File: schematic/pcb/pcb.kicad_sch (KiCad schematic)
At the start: 1 part, among them U1 ESP32-WROOM-32

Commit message: pcb #2
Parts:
- added U2: NEO-M9N, RF_GPS:ublox_NEO, symbol RF_GPS:NEO-M9N
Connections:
- new net: U2.10 (GND), U2.12 (GND), U2.13 (GND), U2.24 (GND)
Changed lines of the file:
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@@
 (kicad_sch (version 20230121) (generator eeschema)
   (paper "A4")
+  (symbol (lib_id "RF_GPS:NEO-M9N") (at 79.375 61.595 0) (unit 1)
+    (in_bom yes) (on_board yes) (dnp no) (fields_autoplaced)
+    (property "Reference" "U2" (at 81.5691 83.82 0)
+      (effects (font (size 1.27 1.27)) (justify left))
+    )
+    (property "Value" "NEO-M9N" (at 81.5691 86.36 0)
+      (effects (font (size 1.27 1.27)) (justify left))
+    )
+    (property "Footprint" "RF_GPS:ublox_NEO" (at 89.535 83.185 0)
+      (effects (font (size 1.27 1.27)) hide)
+    )
+    (property "Datasheet" "https://www.u-blox.com/sites/default/files/NEO-M9N-00B_DataSheet_UBX-19014285.pdf" (at 79.375 61.595 0)
+      (effects (font (size 1.27 1.27)) hide)
+    )
+    (pin "1")
+    (pin "10")
+    (pin "11")
+    (pin "12")
+    (pin "13")
+    (pin "14")
+    (pin "15")
+    (pin "16")
+    (pin "17")
+    (pin "18")
+    (pin "19")
+    (pin "2")
+    (pin "20")
+    (pin "21")
+    (pin "22")
+    (pin "23")
+    (pin "24")
+    (pin "3")
+    (pin "4")
+    (pin "5")
+    (pin "6")
+    (pin "7")
+    (pin "8")
+    (pin "9")
+    (instances
+      (project "pcb"
+        (path "/bb09d15e-8949-465f-96ce-de682ac5520f"
+          (reference "U2") (unit 1)
+        )
+      )
+    )
+  )
   (symbol (lib_id "RF_Module:ESP32-WROOM-32") (at 140.589 62.357 0) (unit 1)
     (in_bom yes) (on_board yes) (dnp no) (fields_autoplaced)

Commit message: schematic update
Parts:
- added C1: 1004322, RF_GPS:GPS_ANTENNA, symbol GPS_ANTENNA:1004322
- added C2: 0.1uH, symbol Device:C_Small
- added C3: 1uH, symbol Device:C_Small
- added P1: USB_C_Plug_USB2.0, Connector_USB:USB_C_Receptacle_GCT_USB4135-GF-A_6P_TopMnt_Horizontal, symbol Connector:USB_C_Plug_USB2.0
- added R1, R10, R11, R12, R13, R14, R15, R16, R17, R18, R2, R3, R4, R5, R6, R7, R8, R9: R_Small, Resistor_SMD:R_0402_1005Metric_Pad0.72x0.64mm_HandSolder, symbol Device:R_Small
- added U3: CP2102N-Axx-xQFN28, Package_DFN_QFN:QFN-28-1EP_5x5mm_P0.5mm_EP3.35x3.35mm, symbol Interface_USB:CP2102N-Axx-xQFN28
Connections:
- net at U2.1 (~{SAFEBOOT}): now also R8.2
- net at U2.10 (GND), U2.12 (GND), U2.13 (GND)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: now also R18.2
- net at U2.11 (RF_IN): now also R16.1
- net at U2.14 (LNA_EN): now also R15.1
- net at U2.18 (SDA/~{SPI_CS}): now also R5.2
- net at U2.19 (SCL/SPI_CLK): now also R6.2
- net at U2.2 (D_SEL): now also R10.2
- net at U2.20 (TXD/SPI_MISO): now also R3.2
- net at U2.21 (RXD/SPI_MOSI): now also R4.2
- net at U2.22 (V_BCKP): now also R12.1
- net at U2.23 (VCC): now also R11.1
- net at U2.3 (TIMEPULSE): now also R17.1
- net at U2.4 (EXTINT): now also R7.2
- net at U2.5 (USB_DM): now also R1.1
- net at U2.6 (USB_DP): now also R2.2
- net at U2.7 (VDD_USB): now also R13.1
- net at U2.8 (~{RESET}): now also R9.2
- net at U2.9 (VCC_RF): now also R14.1
- net GND: now reaches U1.1 (GND), U1.15 (GND), U1.38 (GND), U1.39 (GND)
- net GND: now also C2.1, C3.2, P1.A1 (GND), P1.A12 (GND), P1.B1 (GND), P1.B12 (GND), P1.S1 (SHIELD), R13.2, R18.1, U3.29 (GND), U3.3 (GND)
- net GPS_MISO: now reaches U1.13 (IO14)
- net GPS_MISO: now also R3.1
- net GPS_SCK: now reaches U1.16 (IO13)
- net GPS_SCK: now also R6.1
- net GPS_MOSI: now reaches U1.27 (IO16)
- net GPS_MOSI: now also R4.1
- net ESP32_RX0: now reaches U1.34 (RXD0/IO3)
- net ESP32_RX0: now also U3.26 (TXD)
- net ESP32_TX0: now reaches U1.35 (TXD0/IO1)
- net ESP32_TX0: now also U3.25 (RXD)
- new net: C1.1, R16.2
- new net: C3.1, P1.A4 (VBUS), P1.A9 (VBUS), P1.B4 (VBUS), P1.B9 (VBUS), U3.7 (VREGIN), U3.8 (VBUS)
- new net: P1.A6 (D+), U3.4 (D+)
- new net: P1.A7 (D-), U3.5 (D-)
- new net +3V3: C2.2, R11.2, R12.2, U3.6 (VDD)
- new net GPS_CS: R5.1
- no-connect marks 0 -> 11
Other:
- note added: "ESP32 WROOM 32"
- note added: "UBLOX M9N"
- note added: "USB <-> UART"
- moved on the sheet: U1, U2

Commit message: schematic udpt
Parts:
- added C4: 10uF, symbol Device:C_Small
- added C5, C6: 0.1uF, symbol Device:C_Small
- added J1: MAV_Serial, Connector_JST:JST_GH_BM04B-GHS-TBT_1x04-1MP_P1.25mm_Vertical, symbol Connector:Conn_01x04_Pin
- added J2: Screen, symbol Connector:Conn_01x06_Pin
- added J3: SERVO_Serial, Connector_JST:JST_GH_BM04B-GHS-TBT_1x04-1MP_P1.25mm_Vertical, symbol Connector:Conn_01x04_Pin
- added J4: MAG_Serial, Connector_JST:JST_GH_BM04B-GHS-TBT_1x04-1MP_P1.25mm_Vertical, symbol Connector:Conn_01x04_Pin
- added R19: 10k, symbol Device:R_Small
- added SW1: BOOT, symbol Switch:SW_Push
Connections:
- net +3V3: now also U1.2 (VDD), C4.1, C5.1, R19.1
- net GND: now also C4.2, C5.2, C6.2, SW1.2
- net GPS_CS: now also U1.23 (IO15)
- net GPS_MISO: now also U1.14 (IO12); no longer U1.13 (IO14)
- net GPS_MOSI: now also U1.16 (IO13); no longer U1.27 (IO16)
- net GPS_SCK: now also U1.13 (IO14); no longer U1.16 (IO13)
- net at U1.25 (IO0): now also SW1.1
- net SCREEN_CS: now reaches U1.29 (IO5)
- net at U1.3 (EN): now also C6.1, R19.2
- net SCREEN_SCK: now reaches U1.30 (IO18)
- net SCREEN_MISO: now reaches U1.31 (IO19)
- net SCREEN_MOSI: now reaches U1.37 (IO23)
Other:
- moved on the sheet: C3, U1

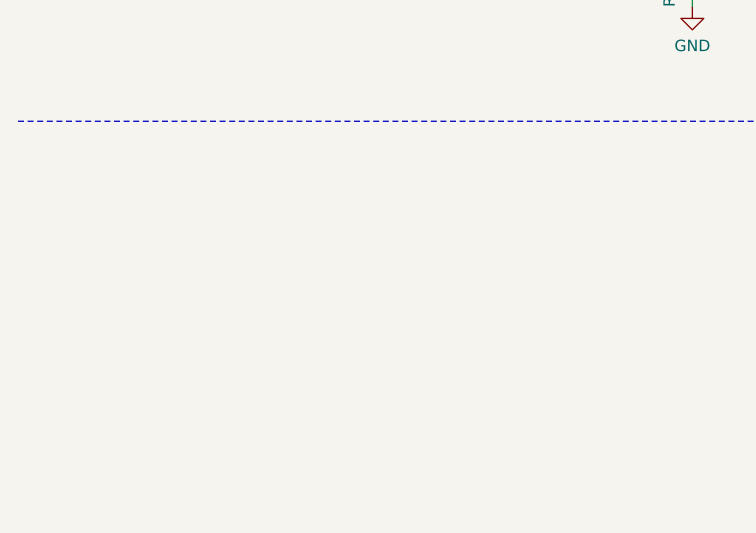
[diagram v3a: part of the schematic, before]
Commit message: ldo added
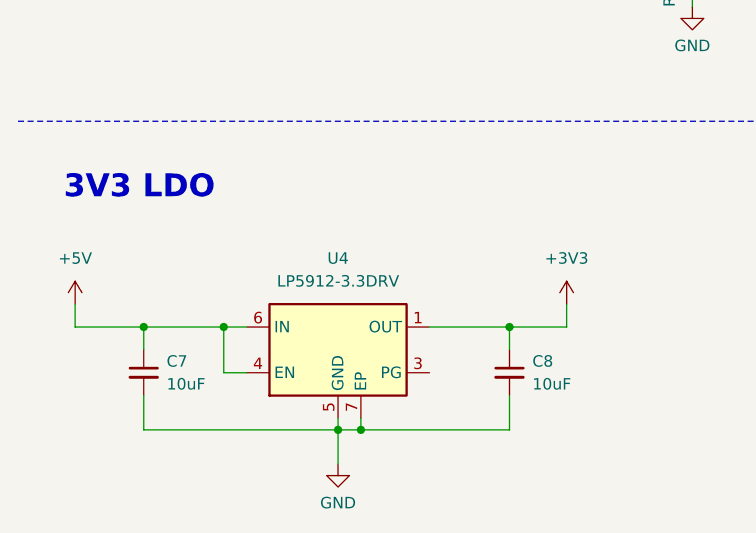
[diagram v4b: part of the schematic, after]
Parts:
- added C7, C8: 10uF, symbol Device:C_Small
- added U4: LP5912-3.3DRV, Package_SON:WSON-6-1EP_2x2mm_P0.65mm_EP1x1.6mm_ThermalVias, symbol Regulator_Linear:LP5912-3.3DRV
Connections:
- net +3V3: now also C8.1, U4.1 (OUT)
- net GND: now also C7.2, C8.2, U4.5 (GND), U4.7 (EP)
- new net +5V: C7.1, U4.4 (EN), U4.6 (IN)
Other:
- note added: "3V3 LDO"
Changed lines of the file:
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@@
   (junction (at 82.55 30.48) (diameter 0) (color 0 0 0 0)
   )
+  (junction (at 67.31 135.89) (diameter 0) (color 0 0 0 0)
+  )
+  (junction (at 48.26 147.32) (diameter 0) (color 0 0 0 0)
+  )
+  (junction (at 50.8 147.32) (diameter 0) (color 0 0 0 0)
+  )
   (junction (at 317.5 83.82) (diameter 0) (color 0 0 0 0)
   )
@@
   )
   (junction (at 204.47 44.45) (diameter 0) (color 0 0 0 0)
+  )
+  (junction (at 26.67 135.89) (diameter 0) (color 0 0 0 0)
+  )
+  (junction (at 35.56 135.89) (diameter 0) (color 0 0 0 0)
   )
   (no_connect (at 332.74 52.07))
@@
     (stroke (width 0) (type default))
   )
+  (wire (pts (xy 67.31 135.89) (xy 67.31 138.43))
+    (stroke (width 0) (type default))
+  )
   (wire (pts (xy 87.63 31.75) (xy 87.63 36.83))
     (stroke (width 0) (type default))
@@
     (stroke (width 0) (type default))
   )
+  (wire (pts (xy 38.1 140.97) (xy 35.56 140.97))
+    (stroke (width 0) (type default))
+  )
   (wire (pts (xy 350.52 34.29) (xy 370.84 34.29))
     (stroke (width 0) (type default))
   )
   (wire (pts (xy 66.04 80.01) (xy 69.85 80.01))
+    (stroke (width 0) (type default))
+  )
+  (wire (pts (xy 67.31 143.51) (xy 67.31 147.32))
     (stroke (width 0) (type default))
   )
@@
     (stroke (width 0) (type dash))
   )
+  (wire (pts (xy 48.26 147.32) (xy 48.26 151.13))
+    (stroke (width 0) (type default))
+  )
+  (wire (pts (xy 58.42 135.89) (xy 67.31 135.89))
+    (stroke (width 0) (type default))
+  )
+  (wire (pts (xy 26.67 143.51) (xy 26.67 147.32))
+    (stroke (width 0) (type default))
+  )
   (wire (pts (xy 172.72 46.99) (xy 185.42 46.99))
     (stroke (width 0) (type default))
@@
     (stroke (width 0) (type default))
   )
+  (wire (pts (xy 50.8 146.05) (xy 50.8 147.32))
+    (stroke (width 0) (type default))
+  )
   (wire (pts (xy 373.38 24.13) (xy 373.38 27.94))
     (stroke (width 0) (type default))
   )
+  (wire (pts (xy 67.31 147.32) (xy 50.8 147.32))
+    (stroke (width 0) (type default))
+  )
+  (wire (pts (xy 48.26 146.05) (xy 48.26 147.32))
+    (stroke (width 0) (type default))
+  )
   (wire (pts (xy 87.63 90.17) (xy 87.63 92.71))
     (stroke (width 0) (type default))
   )
+  (wire (pts (xy 73.66 135.89) (xy 67.31 135.89))
+    (stroke (width 0) (type default))
+  )
   (wire (pts (xy 386.08 41.91) (xy 391.16 41.91))
     (stroke (width 0) (type default))
@@
   )
   (wire (pts (xy 172.72 39.37) (xy 172.72 40.64))
+    (stroke (width 0) (type default))
+  )
+  (wire (pts (xy 26.67 135.89) (xy 26.67 138.43))
     (stroke (width 0) (type default))
   )
@@
     (stroke (width 0) (type default))
   )
+  (wire (pts (xy 35.56 135.89) (xy 26.67 135.89))
+    (stroke (width 0) (type default))
+  )
+  (wire (pts (xy 50.8 147.32) (xy 48.26 147.32))
+    (stroke (width 0) (type default))
+  )
   (polyline (pts (xy 297.18 12.7) (xy 297.18 113.03))
     (stroke (width 0) (type dash))
@@
     (stroke (width 0) (type default))
   )
+  (wire (pts (xy 48.26 147.32) (xy 26.67 147.32))
+    (stroke (width 0) (type default))
+  )
+  (wire (pts (xy 35.56 140.97) (xy 35.56 135.89))
+    (stroke (width 0) (type default))
+  )
   (wire (pts (xy 204.47 50.8) (xy 204.47 53.34))
     (stroke (width 0) (type default))
@@
   )
   (wire (pts (xy 337.82 44.45) (xy 337.82 54.61))
+    (stroke (width 0) (type default))
+  )
+  (wire (pts (xy 73.66 133.35) (xy 73.66 135.89))
     (stroke (width 0) (type default))
   )
@@
     (stroke (width 0) (type default))
   )
+  (wire (pts (xy 19.05 133.35) (xy 19.05 135.89))
+    (stroke (width 0) (type default))
+  )
   (wire (pts (xy 49.53 62.23) (xy 60.96 62.23))
     (stroke (width 0) (type default))
@@
     (stroke (width 0) (type default))
   )
+  (wire (pts (xy 38.1 135.89) (xy 35.56 135.89))
+    (stroke (width 0) (type default))
+  )
   (wire (pts (xy 87.63 41.91) (xy 87.63 44.45))
     (stroke (width 0) (type default))
@@
   )
   (wire (pts (xy 332.74 57.15) (xy 360.68 57.15))
+    (stroke (width 0) (type default))
+  )
+  (wire (pts (xy 19.05 135.89) (xy 26.67 135.89))
     (stroke (width 0) (type default))
   )
@@
   )
   (text "ESP32 WROOM 32" (at 165.1 19.05 0)
+    (effects (font (size 2.54 2.54) (thickness 0.508) bold) (justify left bottom))
+  )
+  (text "3V3 LDO" (at 17.78 121.92 0)
     (effects (font (size 2.54 2.54) (thickness 0.508) bold) (justify left bottom))
   )
@@
     )
   )
+  (symbol (lib_id "Device:C_Small") (at 67.31 140.97 0) (unit 1)
+    (in_bom yes) (on_board yes) (dnp no) (fields_autoplaced)
+    (property "Reference" "C8" (at 69.85 139.7063 0)
+      (effects (font (size 1.27 1.27)) (justify left))
+    )
+    (property "Value" "10uF" (at 69.85 142.2463 0)
+      (effects (font (size 1.27 1.27)) (justify left))
+    )
+    (property "Footprint" "" (at 67.31 140.97 0)
+      (effects (font (size 1.27 1.27)) hide)
+    )
+    (property "Datasheet" "~" (at 67.31 140.97 0)
+      (effects (font (size 1.27 1.27)) hide)
+    )
+    (pin "1")
+    (pin "2")
+    (instances
+      (project "pcb"
+        (path "/bb09d15e-8949-465f-96ce-de682ac5520f"
+          (reference "C8") (unit 1)
+        )
+      )
+    )
+  )
   (symbol (lib_id "Device:C_Small") (at 172.72 43.18 0) (unit 1)
     (in_bom yes) (on_board yes) (dnp no) (fields_autoplaced)
@@
     )
   )
+  (symbol (lib_id "Regulator_Linear:LP5912-3.3DRV") (at 48.26 138.43 0) (unit 1)
+    (in_bom yes) (on_board yes) (dnp no) (fields_autoplaced)
+    (property "Reference" "U4" (at 48.26 128.27 0)
+      (effects (font (size 1.27 1.27)))
+    )
+    (property "Value" "LP5912-3.3DRV" (at 48.26 130.81 0)
+      (effects (font (size 1.27 1.27)))
+    )
+    (property "Footprint" "Package_SON:WSON-6-1EP_2x2mm_P0.65mm_EP1x1.6mm_ThermalVias" (at 48.26 129.54 0)
+      (effects (font (size 1.27 1.27)) hide)
+    )
+    (property "Datasheet" "http://www.ti.com/lit/ds/symlink/lp5912.pdf" (at 48.26 125.73 0)
+      (effects (font (size 1.27 1.27)) hide)
+    )
+    (pin "1")
+    (pin "2")
+    (pin "4")
+    (pin "5")
+    (pin "6")
+    (pin "3")
+    (pin "7")
+    (instances
+      (project "pcb"
+        (path "/bb09d15e-8949-465f-96ce-de682ac5520f"
+          (reference "U4") (unit 1)
+        )
+      )
+    )
+  )
   (symbol (lib_id "power:+3V3") (at 82.55 26.67 0) (unit 1)
     (in_bom yes) (on_board yes) (dnp no) (fields_autoplaced)
@@
         (path "/bb09d15e-8949-465f-96ce-de682ac5520f"
           (reference "C5") (unit 1)
+        )
+      )
+    )
+  )
+  (symbol (lib_id "power:GND") (at 48.26 151.13 0) (unit 1)
+    (in_bom yes) (on_board yes) (dnp no) (fields_autoplaced)
+    (property "Reference" "#PWR017" (at 48.26 157.48 0)
+      (effects (font (size 1.27 1.27)) hide)
+    )
+    (property "Value" "GND" (at 48.26 155.448 0)
+      (effects (font (size 1.27 1.27)))
+    )
+    (property "Footprint" "" (at 48.26 151.13 0)
+      (effects (font (size 1.27 1.27)) hide)
+    )
+    (property "Datasheet" "" (at 48.26 151.13 0)
+      (effects (font (size 1.27 1.27)) hide)
+    )
+    (pin "1")
+    (instances
+      (project "pcb"
+        (path "/bb09d15e-8949-465f-96ce-de682ac5520f"
+          (reference "#PWR017") (unit 1)
         )
       )
@@
         (path "/bb09d15e-8949-465f-96ce-de682ac5520f"
           (reference "U2") (unit 1)
+        )
+      )
+    )
+  )
+  (symbol (lib_id "power:+5V") (at 19.05 133.35 0) (unit 1)
+    (in_bom yes) (on_board yes) (dnp no) (fields_autoplaced)
+    (property "Reference" "#PWR016" (at 19.05 137.16 0)
+      (effects (font (size 1.27 1.27)) hide)
+    )
+    (property "Value" "+5V" (at 19.05 128.27 0)
+      (effects (font (size 1.27 1.27)))
+    )
+    (property "Footprint" "" (at 19.05 133.35 0)
+      (effects (font (size 1.27 1.27)) hide)
+    )
+    (property "Datasheet" "" (at 19.05 133.35 0)
+      (effects (font (size 1.27 1.27)) hide)
+    )
+    (pin "1")
+    (instances
+      (project "pcb"
+        (path "/bb09d15e-8949-465f-96ce-de682ac5520f"
+          (reference "#PWR016") (unit 1)
         )
       )
@@
         (path "/bb09d15e-8949-465f-96ce-de682ac5520f"
           (reference "C2") (unit 1)
+        )
+      )
+    )
+  )
+  (symbol (lib_id "power:+3V3") (at 73.66 133.35 0) (unit 1)
+    (in_bom yes) (on_board yes) (dnp no) (fields_autoplaced)
+    (property "Reference" "#PWR018" (at 73.66 137.16 0)
+      (effects (font (size 1.27 1.27)) hide)
+    )
+    (property "Value" "+3V3" (at 73.66 128.27 0)
+      (effects (font (size 1.27 1.27)))
+    )
+    (property "Footprint" "" (at 73.66 133.35 0)
+      (effects (font (size 1.27 1.27)) hide)
+    )
+    (property "Datasheet" "" (at 73.66 133.35 0)
+      (effects (font (size 1.27 1.27)) hide)
+    )
+    (pin "1")
+    (instances
+      (project "pcb"
+        (path "/bb09d15e-8949-465f-96ce-de682ac5520f"
+          (reference "#PWR018") (unit 1)
         )
       )
@@
         )
       )
+    )
+  )
+  (symbol (lib_id "Device:C_Small") (at 26.67 140.97 0) (unit 1)
+    (in_bom yes) (on_board yes) (dnp no) (fields_autoplaced)
+    (property "Reference" "C7" (at 29.21 139.7063 0)
+      (effects (font (size 1.27 1.27)) (justify left))
+    )
+    (property "Value" "10uF" (at 29.21 142.2463 0)
+      (effects (font (size 1.27 1.27)) (justify left))
+    )
+    (property "Footprint" "" (at 26.67 140.97 0)
+      (effects (font (size 1.27 1.27)) hide)
+    )
+    (property "Datasheet" "~" (at 26.67 140.97 0)
+      (effects (font (size 1.27 1.27)) hide)
+    )
+    (pin "1")
+    (pin "2")
+    (instances
+      (project "pcb"
+        (path "/bb09d15e-8949-465f-96ce-de682ac5520f"
+          (reference "C7") (unit 1)
+        )
+      )

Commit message: schematic update
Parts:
- removed R1, R10, R11, R12, R13, R14, R15, R16, R17, R18, R2, R3, R4, R5, R6, R7, R8, R9: R_Small, Resistor_SMD:R_0402_1005Metric_Pad0.72x0.64mm_HandSolder, symbol Device:R_Small
- added C10, C9: 0.1uF/50V 10%, symbol Device:C_Small
- added Q1, Q2: NPN, symbol Simulation_SPICE:NPN
- added R20, R21: R_Small, symbol Device:R_Small
- added R22: 47.5K 5%, symbol Device:R_Small
- added R23: 2K 5%, symbol Device:R_Small
- added R24: 10K 5% (NC), symbol Device:R_Small
- added R25: 10K 5%, symbol Device:R_Small
- added SW2: SW_Push, symbol Switch:SW_Push
- C2: value 0.1uH -> 0.1uF
- C3: value 1uH -> 4.7uF
- C6: value 0.1uF -> 0.1uF/50V 10%
- J2: value Screen -> Display
- R19: value 10k -> 22.1K 5%
- SW1: value BOOT -> SW_Push
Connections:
- net +3V3: now also C2.1, C3.1, U2.22 (V_BCKP), U2.23 (VCC), U3.7 (VREGIN), R23.1, R25.1; no longer C2.2, R19.1
- net GND: now also C2.2, SW1.1, U2.10 (GND), U2.12 (GND), U2.13 (GND), U2.24 (GND), U2.7 (VDD_USB), C10.1, C9.1, R22.2, R24.2, SW2.1; no longer C2.1, SW1.2
- net GPS_CS: now also U2.18 (SDA/~{SPI_CS})
- net GPS_MISO: now also U2.20 (TXD/SPI_MISO)
- net GPS_MOSI: now also U2.21 (RXD/SPI_MOSI)
- net GPS_SCK: now also U2.19 (SCL/SPI_CLK)
- net EN: now reaches C6.1, U1.3 (EN)
- net EN: now also C10.2, Q1.1 (C), R25.2, SW2.2; no longer R19.2
- net at C1.1: now also U2.11 (RF_IN)
- net VBUS: now reaches P1.A4 (VBUS), P1.A9 (VBUS), P1.B4 (VBUS), P1.B9 (VBUS)
- net VBUS: now also R19.1; no longer C3.1, U3.7 (VREGIN), U3.8 (VBUS)
- net USB_D+: now reaches P1.A6 (D+), U3.4 (D+)
- net USB_D-: now reaches P1.A7 (D-), U3.5 (D-)
- net IO0: now reaches U1.25 (IO0)
- net IO0: now also SW1.2, C9.2, Q2.1 (C); no longer SW1.1
- net DCD: now reaches U3.1 (~{DCD})
- net at U3.11 (~{SUSPEND}): now also R24.1
- net RI: now reaches U3.2 (~{RI}/CLK)
- net CTS: now reaches U3.23 (~{CTS})
- net RTS: now reaches U3.24 (~{RTS})
- net RTS: now also Q1.3 (E), R21.2
- net DSR: now reaches U3.27 (~{DSR})
- net DTR: now reaches U3.28 (~{DTR})
- net DTR: now also Q2.3 (E), R20.2
- net at U3.9 (~{RST}): now also R23.2
- new net: R19.2, R22.1, U3.8 (VBUS)
- new net: Q1.2 (B), R20.1
- new net: Q2.2 (B), R21.1
- no-connect marks 11 -> 22
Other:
- note added: "* Ekran * Magnetometr * Serial serwo * Serwo * RX * 5V"
- moved on the sheet: C1, C2, C4, C5, C7, C8, J1, J2, J3, J4, P1, U1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

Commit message: updt
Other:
- note added: "3.3 LDO"
- note added: "CP2102"
- note removed: "3V3 LDO"
- note removed: "USB <-> UART"
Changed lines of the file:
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@@
     (fill (type none))
   )
-  (text "USB <-> UART" (at 83.82 18.415 0)
+  (text "CP2102" (at 83.82 18.415 0)
     (effects (font (size 2.54 2.54) (thickness 0.508) bold) (justify left bottom))
   )
@@
     (effects (font (size 2.54 2.54) (thickness 0.508) bold) (justify left bottom))
   )
-  (text "3V3 LDO" (at 14.605 17.78 0)
+  (text "3.3 LDO" (at 14.605 17.78 0)
     (effects (font (size 2.54 2.54) (thickness 0.508) bold) (justify left bottom))
   )

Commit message: updt
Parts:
- removed J2: Display, symbol Connector:Conn_01x06_Pin
- added J2: Display, Connector_JST:JST_GH_BM05B-GHS-TBT_1x05-1MP_P1.25mm_Vertical, symbol Connector:Conn_01x05_Pin
- added J5: Servo, Connector_JST:JST_GH_BM03B-GHS-TBT_1x03-1MP_P1.25mm_Vertical, symbol Connector:Conn_01x03_Pin
- C10, C2, C3, C4, C5, C6, C7, C8, C9: footprint (none) -> Capacitor_SMD:C_0805_2012Metric
- Q1, Q2: footprint (none) -> Package_TO_SOT_SMD:TSOT-23
- R19, R22, R23, R25: footprint (none) -> Resistor_SMD:R_0805_2012Metric
- R20, R21: value R_Small -> 10K 5%; footprint (none) -> Resistor_SMD:R_0805_2012Metric
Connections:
- net +5V is gone; now on net VBUS: C7.1, U4.4 (EN), U4.6 (IN)
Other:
- note added: "https://dl.espressif.com/dl/schematics/esp32_devkitc_v4-sch.pdf"
- title: (none) -> Główna płytka
- moved on the sheet: J4

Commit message: pcb update
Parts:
- added J6: 5V, Connector_Wuerth:Wuerth_WR-WTB_64800211622_1x02_P1.50mm_Vertical, symbol Connector:Conn_01x02_Pin
- J1: value MAV_Serial -> MAVLINK
- J2: value Display -> DISPLAY
- J3: value SERVO_Serial -> SER. SERVO
- J4: value MAG_Serial -> MAG.
- J5: value Servo -> SERVO; footprint Connector_JST:JST_GH_BM03B-GHS-TBT_1x03-1MP_P1.25mm_Vertical -> Connector_PinHeader_2.54mm:PinHeader_1x03_P2.54mm_Vertical
- R6: renamed from R24; footprint (none) -> Resistor_SMD:R_0805_2012Metric
- renumbered C7 to C1, C5 to C10, C8 to C2, C1 to C3, C2 to C4, C3 to C5, C4 to C6, C6 to C7, C9 to C8, C10 to C9, U3 to CP1, U1 to ESP1, U4 to LDO1, R21 to R1, R20 to R2, R19 to R3, R22 to R4, R23 to R5, R25 to R7, U2 to U1
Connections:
- net VBUS is gone; now on net +5V: C1.1, LDO1.4 (EN), LDO1.6 (IN), P1.A4 (VBUS), P1.A9 (VBUS), P1.B4 (VBUS), P1.B9 (VBUS), R3.1
- net GND: now also J5.1 (Pin_1), J6.2 (Pin_2)
- net +5V: now reaches J5.3 (Pin_3)
- net +5V: now also J6.1 (Pin_1)
